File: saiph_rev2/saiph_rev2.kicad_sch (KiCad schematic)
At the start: 208 parts, among them J1 USB_mini_micro_B, J2 Conn_01x04, SW1 SW_PUSH, SW10 SW_PUSH, SW100 SW_PUSH, SW101 SW_PUSH, SW102 SW_PUSH, SW103 SW_PUSH, SW104 SW_PUSH, SW105 SW_PUSH, SW109 SW_PUSH, SW11 SW_PUSH, SW110 SW_PUSH, SW111 SW_PUSH, SW12 SW_PUSH, SW13 SW_PUSH, SW14 SW_PUSH, SW15 SW_PUSH, SW16 SW_PUSH, SW17 SW_PUSH, SW18 SW_PUSH, SW19 SW_PUSH, SW2 SW_PUSH, SW20 SW_PUSH, SW21 SW_PUSH, SW22 SW_PUSH, SW23 SW_PUSH, SW24 SW_PUSH, SW25 SW_PUSH, SW26 SW_PUSH, SW27 SW_PUSH, SW28 SW_PUSH, SW29 SW_PUSH, SW3 SW_PUSH, SW30 SW_PUSH, SW31 SW_PUSH, SW32 SW_PUSH, SW33 SW_PUSH, SW34 SW_PUSH, SW35 SW_PUSH, SW36 SW_PUSH, SW37 SW_PUSH, SW38 SW_PUSH, SW39 SW_PUSH, SW4 SW_PUSH, SW40 SW_PUSH, SW41 SW_PUSH, SW42 SW_PUSH, SW43 SW_PUSH, SW44 SW_PUSH, SW45 SW_PUSH, SW46 SW_PUSH, SW47 SW_PUSH, SW48 SW_PUSH, SW49 SW_PUSH, SW5 SW_PUSH, SW50 SW_PUSH, SW51 SW_PUSH, SW52 SW_PUSH, SW53 SW_PUSH, SW54 SW_PUSH, SW55 SW_PUSH, SW56 SW_PUSH, SW57 SW_PUSH, SW58 SW_PUSH, SW59 SW_PUSH, SW6 SW_PUSH, SW60 SW_PUSH, SW61 SW_PUSH, SW62 SW_PUSH, SW63 SW_PUSH, SW64 SW_PUSH, SW65 SW_PUSH, SW66 SW_PUSH, SW67 SW_PUSH, SW68 SW_PUSH, SW69 SW_PUSH, SW7 SW_PUSH, SW70 SW_PUSH, SW71 SW_PUSH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

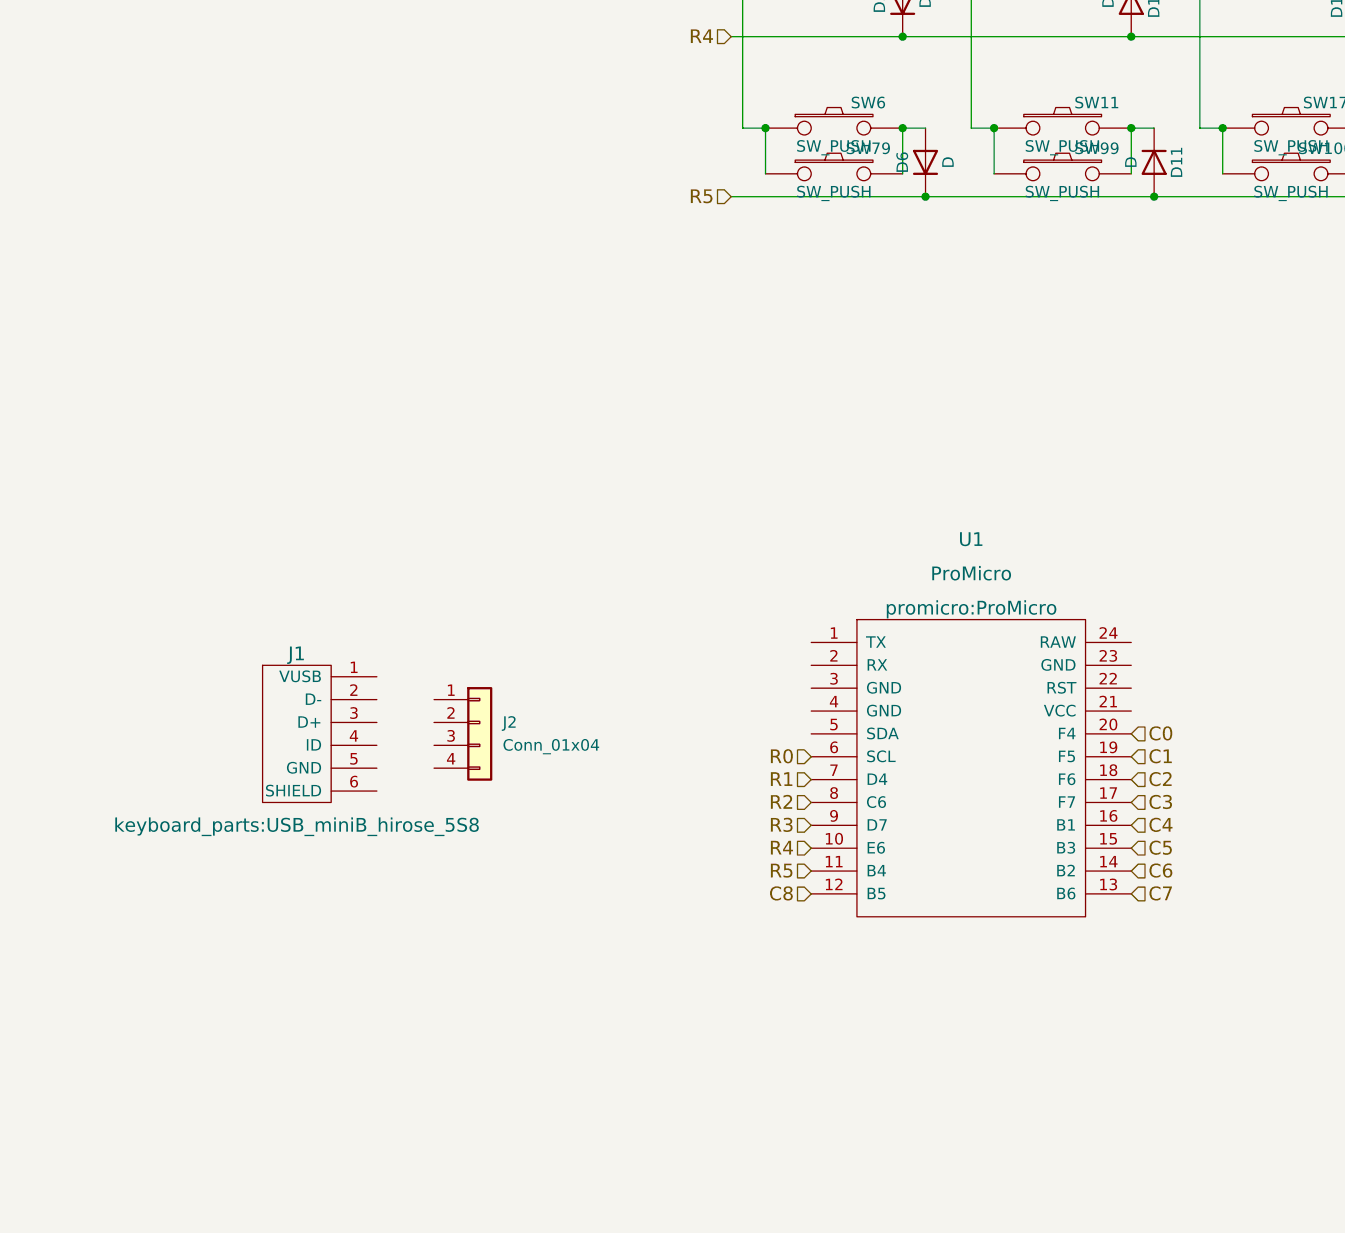
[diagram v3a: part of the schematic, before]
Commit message: place rp2040 stamp and buttons; start planning routing
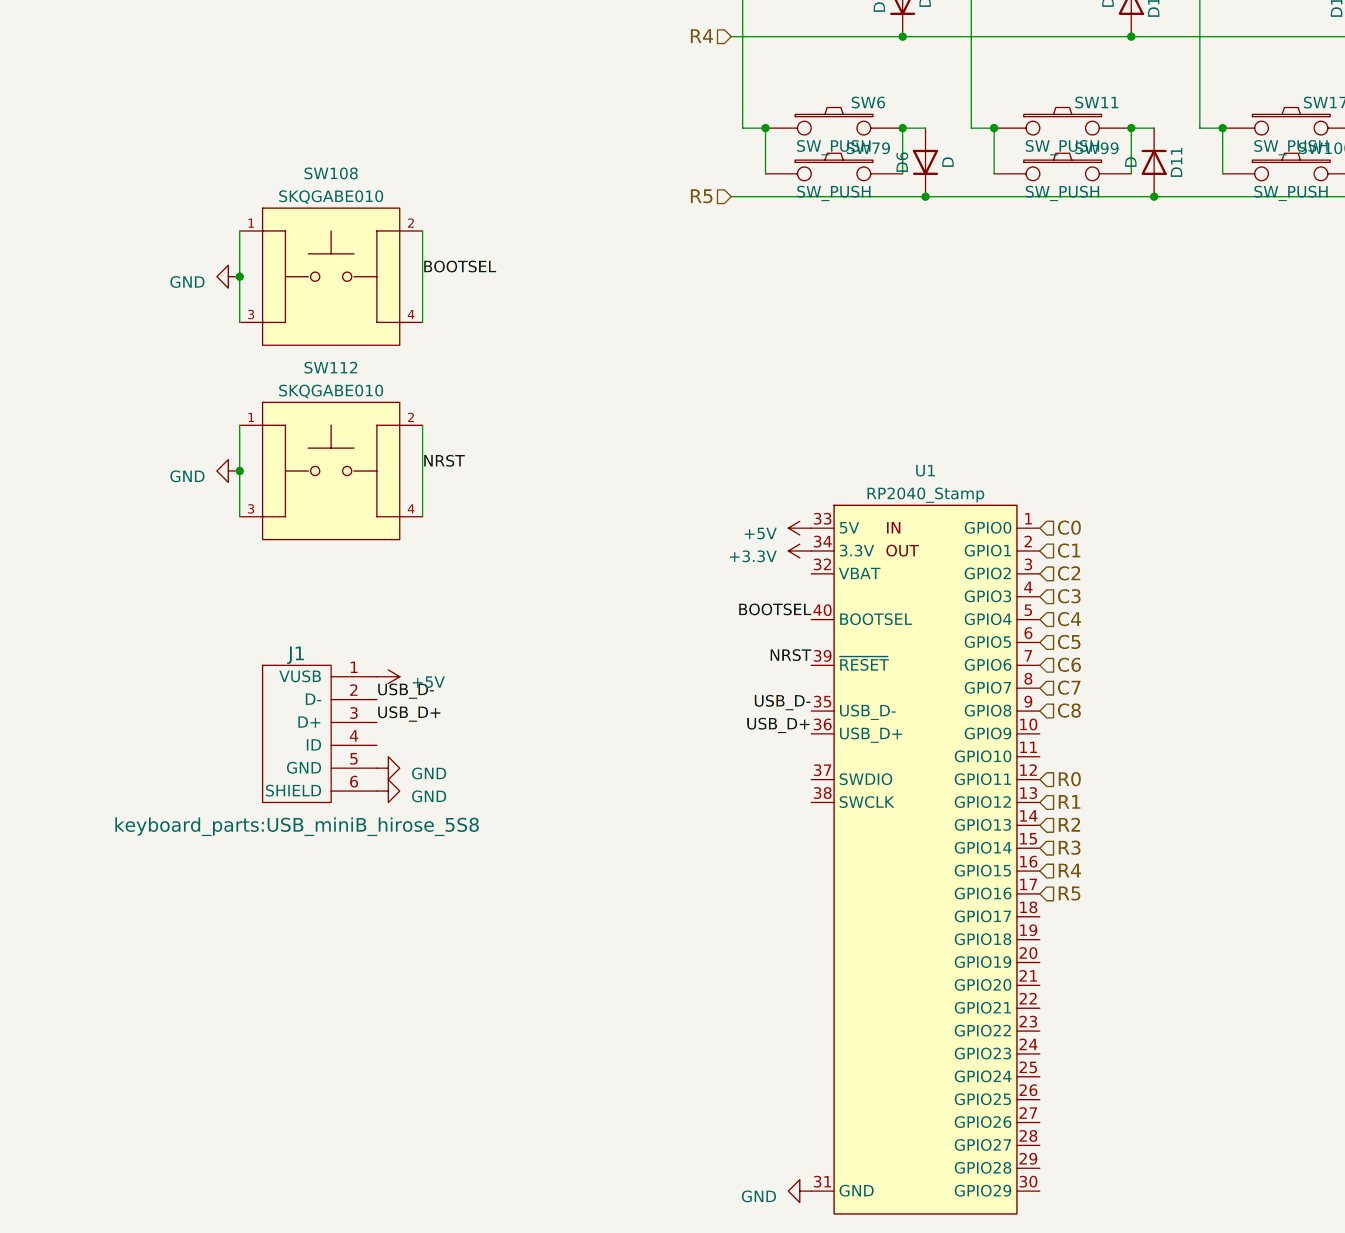
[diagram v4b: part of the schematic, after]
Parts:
- removed J2: Conn_01x04, Connector_PinHeader_2.54mm:PinHeader_1x04_P2.54mm_Vertical, symbol Connector_Generic:Conn_01x04
- removed U1: ProMicro, promicro:ProMicro, symbol promicro:ProMicro
- added SW108, SW112: SKQGABE010, custom_parts:Switch_ALPS_SKQGABE010, symbol Switch_ALPS_SKQGABE010:SKQGABE010
- added U1: RP2040_Stamp, RP2040_Stamp:RP2040_Stamp_SMD, symbol RP2040_Stamp:RP2040_Stamp
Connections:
- net C0: now also U1.1 (GPIO0)
- net C1: now also U1.2 (GPIO1)
- net C2: now also U1.3 (GPIO2)
- net C3: now also U1.4 (GPIO3)
- net C4: now also U1.5 (GPIO4)
- net C5: now also U1.6 (GPIO5)
- net C6: now also U1.7 (GPIO6)
- net C7: now also U1.8 (GPIO7)
- net C8: now also U1.9 (GPIO8)
- net R0: now also U1.12 (GPIO11)
- net R1: now also U1.13 (GPIO12)
- net R2: now also U1.14 (GPIO13)
- net R3: now also U1.15 (GPIO14)
- net R4: now also U1.16 (GPIO15)
- net R5: now also U1.17 (GPIO16)
- net +5V: now reaches J1.1 (VUSB)
- net +5V: now also U1.33 (5V)
- net USB_D-: now reaches J1.2 (D-)
- net USB_D-: now also U1.35 (USB_D-)
- net USB_D+: now reaches J1.3 (D+)
- net USB_D+: now also U1.36 (USB_D+)
- net GND: now reaches J1.5 (GND)
- net GND: now also J1.6 (SHIELD), SW108.1, SW108.3, SW112.1, SW112.3, U1.31 (GND)
- new net +3.3V: U1.34 (3.3V)
- new net BOOTSEL: SW108.2, SW108.4, U1.40 (BOOTSEL)
- new net NRST: SW112.2, SW112.4, U1.39 (~{RESET})

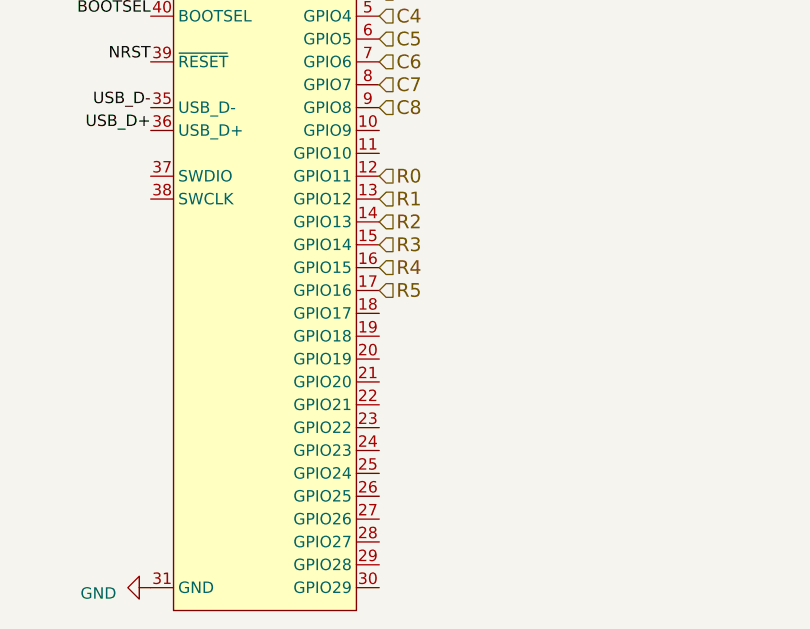
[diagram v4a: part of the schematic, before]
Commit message: add usb traces
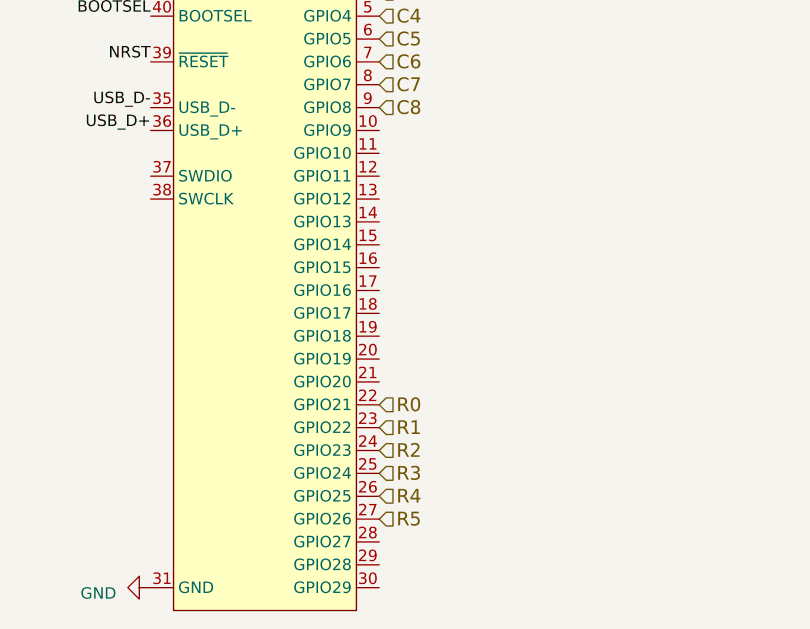
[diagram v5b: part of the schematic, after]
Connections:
- net R0: now also U1.22 (GPIO21); no longer U1.12 (GPIO11)
- net R1: now also U1.23 (GPIO22); no longer U1.13 (GPIO12)
- net R2: now also U1.24 (GPIO23); no longer U1.14 (GPIO13)
- net R3: now also U1.25 (GPIO24); no longer U1.15 (GPIO14)
- net R4: now also U1.26 (GPIO25); no longer U1.16 (GPIO15)
- net R5: now also U1.27 (GPIO26); no longer U1.17 (GPIO16)
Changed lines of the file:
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@@
     (effects (font (size 1.524 1.524)) (justify left))
   )
-  (hierarchical_label "R3" (shape input) (at 143.51 207.01 0) (fields_autoplaced)
+  (hierarchical_label "R5" (shape input) (at 143.51 237.49 0) (fields_autoplaced)
     (effects (font (size 1.524 1.524)) (justify left))
   )
@@
     (effects (font (size 1.524 1.524)) (justify left))
   )
-  (hierarchical_label "R2" (shape input) (at 143.51 204.47 0) (fields_autoplaced)
+  (hierarchical_label "R1" (shape input) (at 143.51 227.33 0) (fields_autoplaced)
+    (effects (font (size 1.524 1.524)) (justify left))
+  )
+  (hierarchical_label "R0" (shape input) (at 143.51 224.79 0) (fields_autoplaced)
     (effects (font (size 1.524 1.524)) (justify left))
   )
@@
     (effects (font (size 1.524 1.524)) (justify left))
   )
-  (hierarchical_label "R1" (shape input) (at 143.51 201.93 0) (fields_autoplaced)
+  (hierarchical_label "R3" (shape input) (at 143.51 232.41 0) (fields_autoplaced)
+    (effects (font (size 1.524 1.524)) (justify left))
+  )
+  (hierarchical_label "R4" (shape input) (at 143.51 234.95 0) (fields_autoplaced)
     (effects (font (size 1.524 1.524)) (justify left))
   )
   (hierarchical_label "R0" (shape input) (at 109.22 45.72 180) (fields_autoplaced)
     (effects (font (size 1.524 1.524)) (justify right))
-  )
-  (hierarchical_label "R0" (shape input) (at 143.51 199.39 0) (fields_autoplaced)
-    (effects (font (size 1.524 1.524)) (justify left))
-  )
-  (hierarchical_label "R4" (shape input) (at 143.51 209.55 0) (fields_autoplaced)
-    (effects (font (size 1.524 1.524)) (justify left))
   )
   (hierarchical_label "C8" (shape input) (at 516.89 33.02 90) (fields_autoplaced)
@@
     (effects (font (size 1.524 1.524)) (justify right))
   )
+  (hierarchical_label "R2" (shape input) (at 143.51 229.87 0) (fields_autoplaced)
+    (effects (font (size 1.524 1.524)) (justify left))
+  )
   (hierarchical_label "C6" (shape input) (at 143.51 186.69 0) (fields_autoplaced)
     (effects (font (size 1.524 1.524)) (justify left))
@@
     (effects (font (size 1.524 1.524)) (justify right))
   )
-  (hierarchical_label "R5" (shape input) (at 143.51 212.09 0) (fields_autoplaced)
-    (effects (font (size 1.524 1.524)) (justify left))
-  )
   (hierarchical_label "C1" (shape input) (at 143.51 173.99 0) (fields_autoplaced)

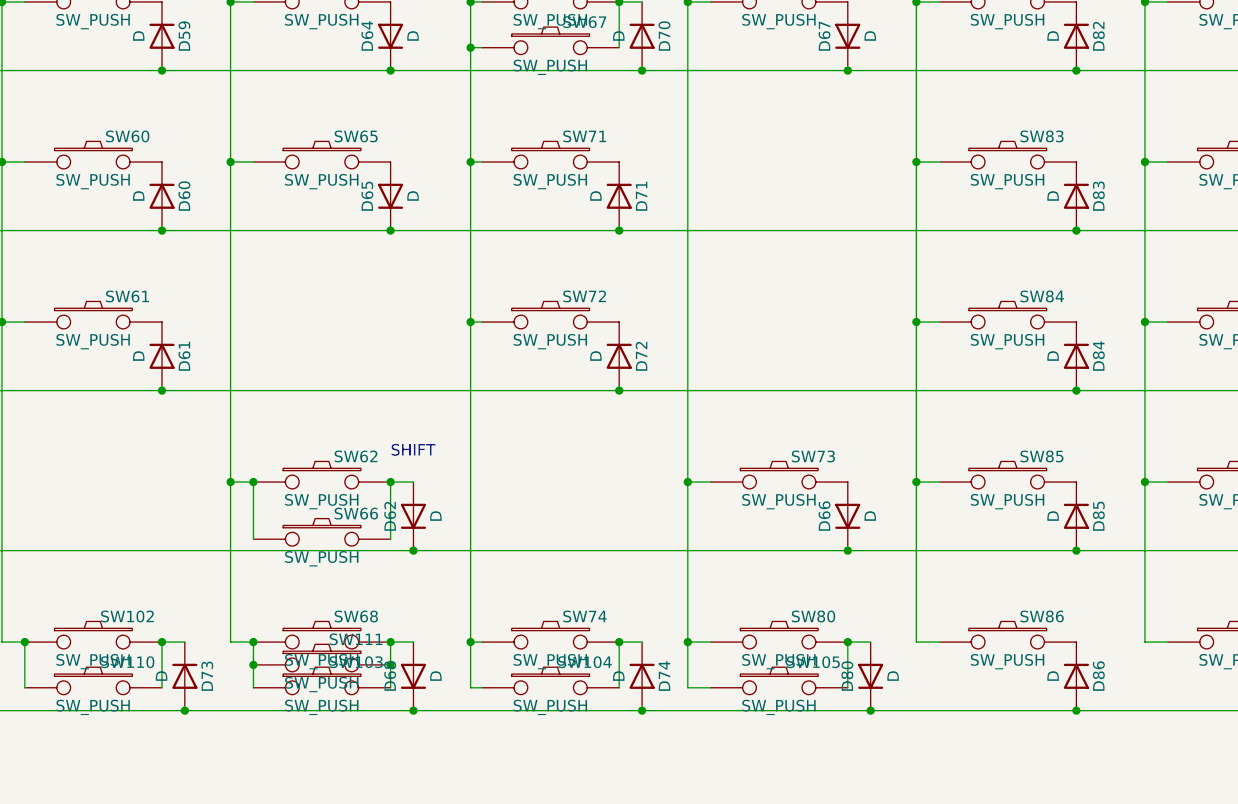
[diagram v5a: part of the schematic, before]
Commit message: place r4 diodes
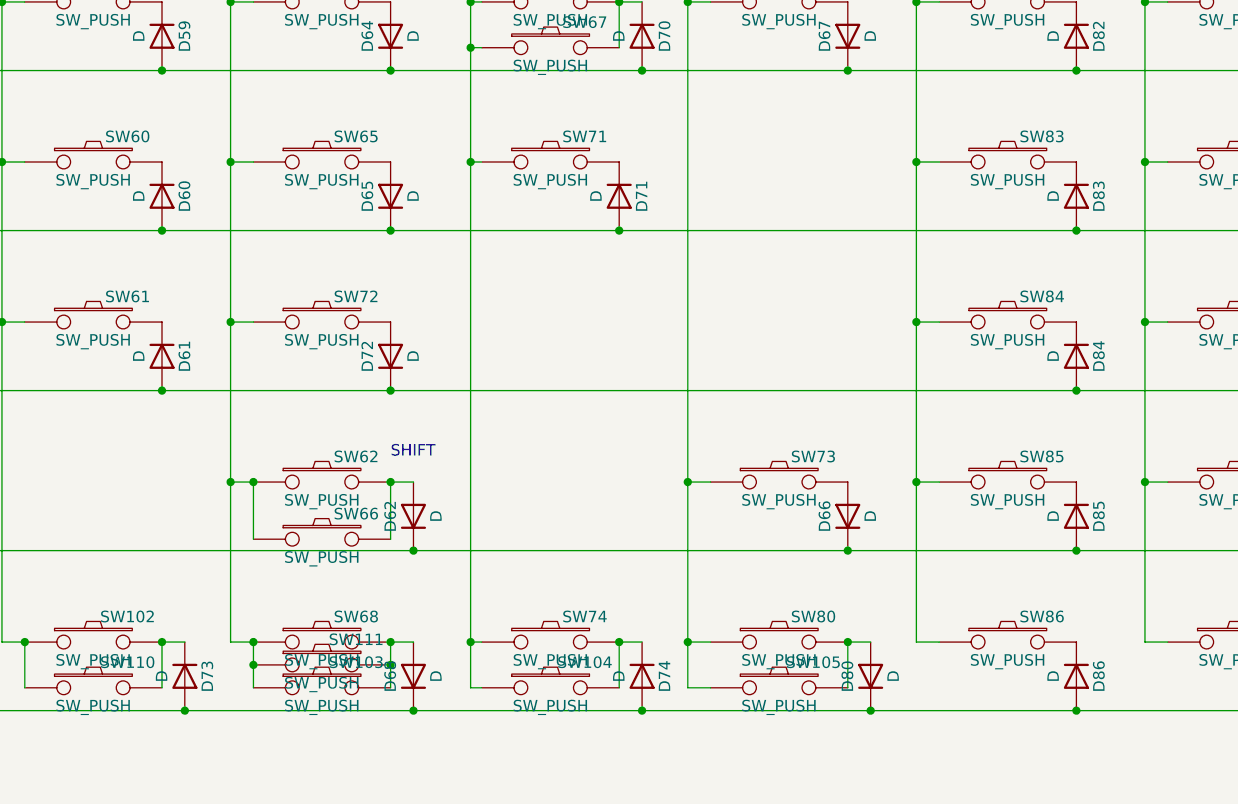
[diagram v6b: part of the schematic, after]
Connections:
- net R3: now also D72.1 (K); no longer D72.2 (A)
- net at SW72.2: now also D72.2 (A); no longer D72.1 (K)
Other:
- moved on the sheet: D72, SW72
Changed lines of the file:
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@@
   (junction (at 356.87 45.72) (diameter 0) (color 0 0 0 0)
   )
-  (junction (at 458.47 99.06) (diameter 0) (color 0 0 0 0)
-  )
   (junction (at 407.67 63.5) (diameter 0) (color 0 0 0 0)
   )
@@
   (junction (at 466.09 109.22) (diameter 0) (color 0 0 0 0)
   )
-  (junction (at 441.96 91.44) (diameter 0) (color 0 0 0 0)
-  )
   (junction (at 135.89 91.44) (diameter 0) (color 0 0 0 0)
   )
@@
   (junction (at 466.09 55.88) (diameter 0) (color 0 0 0 0)
   )
+  (junction (at 415.29 91.44) (diameter 0) (color 0 0 0 0)
+  )
   (junction (at 441.96 127) (diameter 0) (color 0 0 0 0)
   )
@@
   (junction (at 461.01 134.62) (diameter 0) (color 0 0 0 0)
   )
+  (junction (at 433.07 99.06) (diameter 0) (color 0 0 0 0)
+  )
   (junction (at 407.67 45.72) (diameter 0) (color 0 0 0 0)
   )
@@
     (stroke (width 0) (type default))
   )
-  (wire (pts (xy 407.67 99.06) (xy 458.47 99.06))
-    (stroke (width 0) (type default))
-  )
   (wire (pts (xy 186.69 55.88) (xy 186.69 73.66))
     (stroke (width 0) (type default))
@@
     (stroke (width 0) (type default))
   )
+  (wire (pts (xy 415.29 91.44) (xy 417.83 91.44))
+    (stroke (width 0) (type default))
+  )
   (wire (pts (xy 288.29 109.22) (xy 290.83 109.22))
     (stroke (width 0) (type default))
@@
     (stroke (width 0) (type default))
   )
+  (wire (pts (xy 433.07 99.06) (xy 509.27 99.06))
+    (stroke (width 0) (type default))
+  )
   (wire (pts (xy 262.89 91.44) (xy 265.43 91.44))
     (stroke (width 0) (type default))
@@
     (stroke (width 0) (type default))
   )
-  (wire (pts (xy 441.96 91.44) (xy 441.96 127))
+  (wire (pts (xy 441.96 73.66) (xy 441.96 127))
     (stroke (width 0) (type default))
   )
@@
     (stroke (width 0) (type default))
   )
-  (wire (pts (xy 415.29 73.66) (xy 415.29 109.22))
+  (wire (pts (xy 415.29 73.66) (xy 415.29 91.44))
     (stroke (width 0) (type default))
   )
@@
     (stroke (width 0) (type default))
   )
-  (wire (pts (xy 458.47 99.06) (xy 509.27 99.06))
+  (wire (pts (xy 407.67 99.06) (xy 433.07 99.06))
     (stroke (width 0) (type default))
   )
@@
     (stroke (width 0) (type default))
   )
-  (wire (pts (xy 441.96 73.66) (xy 441.96 91.44))
-    (stroke (width 0) (type default))
-  )
   (wire (pts (xy 389.89 73.66) (xy 389.89 91.44))
     (stroke (width 0) (type default))
@@
     (stroke (width 0) (type default))
   )
-  (wire (pts (xy 441.96 91.44) (xy 443.23 91.44))
-    (stroke (width 0) (type default))
-  )
   (wire (pts (xy 364.49 91.44) (xy 367.03 91.44))
     (stroke (width 0) (type default))
@@
     (stroke (width 0) (type default))
   )
+  (wire (pts (xy 415.29 91.44) (xy 415.29 109.22))
+    (stroke (width 0) (type default))
+  )
   (wire (pts (xy 441.96 73.66) (xy 443.23 73.66))
     (stroke (width 0) (type default))
@@
     )
   )
-  (symbol (lib_id "keyboard_parts:SW_PUSH") (at 450.85 91.44 0) (unit 1)
+  (symbol (lib_id "keyboard_parts:SW_PUSH") (at 425.45 91.44 0) (unit 1)
     (in_bom yes) (on_board yes) (dnp no)
-    (property "Reference" "SW72" (at 454.66 88.646 0)
+    (property "Reference" "SW72" (at 429.26 88.646 0)
       (effects (font (size 1.27 1.27)))
     )
-    (property "Value" "SW_PUSH" (at 450.85 93.472 0)
+    (property "Value" "SW_PUSH" (at 425.45 93.472 0)
       (effects (font (size 1.27 1.27)))
     )
-    (property "Footprint" "keyboard_parts:ALPS_PLATE" (at 450.85 91.44 0)
+    (property "Footprint" "keyboard_parts:ALPS_PLATE" (at 425.45 91.44 0)
       (effects (font (size 1.27 1.27)) hide)
     )
-    (property "Datasheet" "" (at 450.85 91.44 0)
+    (property "Datasheet" "" (at 425.45 91.44 0)
       (effects (font (size 1.27 1.27)))
     )
@@
     )
   )
-  (symbol (lib_id "Diode:1N4148") (at 458.47 95.25 270) (unit 1)
+  (symbol (lib_id "Diode:1N4148") (at 433.07 95.25 90) (unit 1)
     (in_bom yes) (on_board yes) (dnp no)
-    (property "Reference" "D72" (at 461.01 95.25 0)
+    (property "Reference" "D72" (at 430.53 95.25 0)
       (effects (font (size 1.27 1.27)))
     )
-    (property "Value" "D" (at 455.93 95.25 0)
+    (property "Value" "D" (at 435.61 95.25 0)
       (effects (font (size 1.27 1.27)))
     )
-    (property "Footprint" "Diodes_ThroughHole:D_DO-35_SOD27_P7.62mm_Horizontal" (at 458.47 95.25 0)
+    (property "Footprint" "Diodes_ThroughHole:D_DO-35_SOD27_P7.62mm_Horizontal" (at 433.07 95.25 0)
       (effects (font (size 1.27 1.27)) hide)
     )
-    (property "Datasheet" "" (at 458.47 95.25 0)
+    (property "Datasheet" "" (at 433.07 95.25 0)
       (effects (font (size 1.27 1.27)))
     )
